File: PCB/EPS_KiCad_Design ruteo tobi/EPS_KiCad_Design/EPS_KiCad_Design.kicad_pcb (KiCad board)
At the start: 4 copper layers, 90 x 90.2 mm, 137 parts, among them IC1 INA226AIDGST, IC10 TPS2553QDBVRQ1, IC11 INA226AIDGST, IC2 TPS2553QDBVRQ1, IC3 INA226AIDGST, IC4 TPS2553QDBVRQ1, IC5 AP63205WU-7, IC6 STM32L433CBT7, IC7 LT3652IMSE#PBF, IC8 INA226AIDGST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

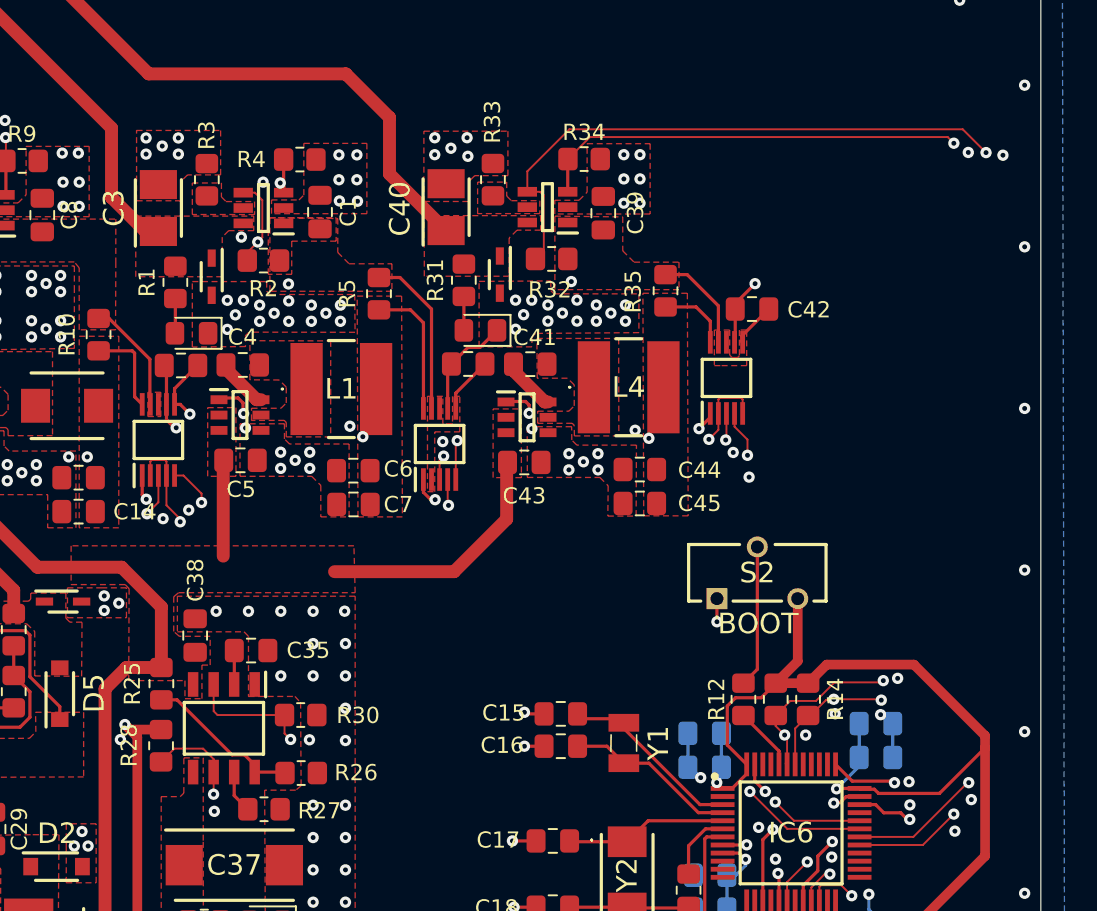
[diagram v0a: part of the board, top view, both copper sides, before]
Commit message: Agregue nombres al pcb
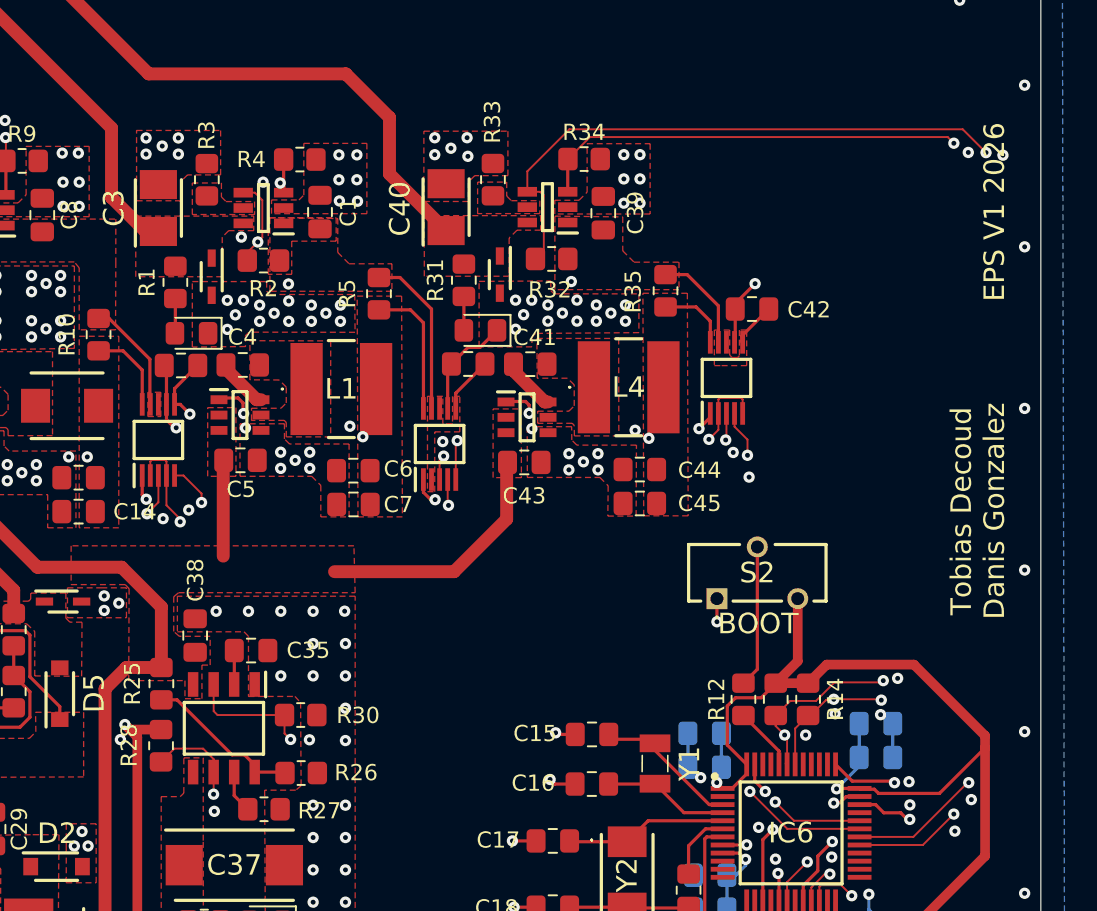
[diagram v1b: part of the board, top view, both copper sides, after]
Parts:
- moved C16 3.03 mm to (162.2, 117.2)
- moved Y1 2.31 mm to (166.1, 116.0)
- moved C15 2.31 mm to (162.2, 114.2)
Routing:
- net /MCU/PC15: track 10.7 -> 7.88 mm
- net /MCU/PC14: track 11.6 -> 9.17 mm
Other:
- board text added: "EPS V1 2026"
- board text added: "Tobias Decoud Danis Gonzalez"
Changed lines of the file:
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@@
 	(footprint "ABS07-LR-32.768KHZ-6-1-T_Footprint:ABS07LR32768kHz61T"
 		(layer "F.Cu")
-		(at 164.2 114.7 -90)
+		(at 166.13 115.97 -90)
 		(descr "ABS07-LR-32.768kHz-6-1-T-2")
 		(tags "Crystal or Oscillator")
@@
 	(footprint "Capacitor_SMD:C_0805_2012Metric_Pad1.18x1.45mm_HandSolder"
 		(layer "F.Cu")
-		(at 160.3 112.9)
+		(at 162.23 114.17)
 		(descr "Capacitor SMD 0805 (2012 Metric), square (rectangular) end terminal, IPC-7351 nominal with elongated pad for handsoldering. (Body size source: IPC-SM-782 page 76, https://www.pcb-3d.com/wordpress/wp-content/uploads/ipc-sm-782a_amendment_1_and_2.pdf, https://docs.google.com/spreadsheets/d/1BsfQQcO9C6DZCsRaXUlFlo91Tg2WpOkGARC1WS5S8t0/edit?usp=sharing), generated with kicad-footprint-generator")
 		(tags "capacitor handsolder")
@@
 	(footprint "Capacitor_SMD:C_0805_2012Metric_Pad1.18x1.45mm_HandSolder"
 		(layer "F.Cu")
-		(at 160.3 114.9)
+		(at 162.22 117.24)
 		(descr "Capacitor SMD 0805 (2012 Metric), square (rectangular) end terminal, IPC-7351 nominal with elongated pad for handsoldering. (Body size source: IPC-SM-782 page 76, https://www.pcb-3d.com/wordpress/wp-content/uploads/ipc-sm-782a_amendment_1_and_2.pdf, https://docs.google.com/spreadsheets/d/1BsfQQcO9C6DZCsRaXUlFlo91Tg2WpOkGARC1WS5S8t0/edit?usp=sharing), generated with kicad-footprint-generator")
 		(tags "capacitor handsolder")
@@
 		)
 	)
+	(gr_text "EPS V1 2026"
+		(at 187.13 81.84 90)
+		(layer "F.SilkS")
+		(effects
+			(font
+				(size 1.27 1.27)
+				(thickness 0.254)
+			)
+		)
+	)
 	(gr_text "3V3"
 		(at 177.92 141.961905 90)
@@
 		)
 	)
+	(gr_text "Tobias Decoud\nDanis Gonzalez"
+		(at 186.107685 100.35 90)
+		(layer "F.SilkS")
+		(effects
+			(font
+				(size 1.27 1.27)
+				(thickness 0.254)
+			)
+		)
+	)
 	(gr_text "EN\nOBC"
 		(at 156.46 67.69 0)
@@
 	)
 	(segment
+		(start 161.1825 117.24)
+		(end 159.92 117.24)
+		(width 0.2)
+		(layer "F.Cu")
+		(net 14)
+	)
+	(segment
 		(start 185.08 127.99)
 		(end 185.09 127.98)
@@
 	)
 	(segment
-		(start 158.15 112.9)
-		(end 158.05 112.8)
+		(start 160.08 114.17)
+		(end 159.98 114.07)
 		(width 0.2)
 		(layer "F.Cu")
@@
 	)
 	(segment
-		(start 159.2625 114.9)
-		(end 158.05 114.9)
-		(width 0.2)
-		(layer "F.Cu")
-		(net 14)
-	)
-	(segment
 		(start 136.501415 95.2)
 		(end 136.398 95.2)
@@
 	)
 	(segment
-		(start 159.2625 112.9)
-		(end 158.15 112.9)
+		(start 159.92 117.24)
+		(end 159.64 116.96)
+		(width 0.2)
+		(layer "F.Cu")
+		(net 14)
+	)
+	(segment
+		(start 161.1925 114.17)
+		(end 160.08 114.17)
 		(width 0.2)
 		(layer "F.Cu")
@@
 	)
 	(via
-		(at 158.05 114.9)
+		(at 159.64 116.96)
 		(size 0.7)
 		(drill 0.3)
@@
 	)
 	(via
-		(at 158.05 112.8)
+		(at 159.98 114.07)
 		(size 0.7)
 		(drill 0.3)
@@
 	)
 	(segment
-		(start 133.93 90.58)
-		(end 133.785 90.435)
+		(start 134.4 91.62)
+		(end 133.215 90.435)
 		(width 0.2)
 		(layer "F.Cu")
@@
 	(segment
 		(start 134.4 93.75)
-		(end 133.93 93.28)
+		(end 134.4 91.62)
 		(width 0.2)
 		(layer "F.Cu")
@@
 	)
 	(segment
-		(start 133.785 90.435)
+		(start 133.215 90.435)
 		(end 131.7 90.435)
 		(width 0.2)
@@
 	)
 	(segment
-		(start 133.93 93.28)
-		(end 133.93 90.58)
-		(width 0.2)
-		(layer "F.Cu")
-		(net 22)
-	)
-	(segment
 		(start 122.85 93.835)
 		(end 123.185 93.835)
@@
 	)
 	(segment
-		(start 164.2 113.45)
-		(end 163.95 113.2)
+		(start 166.13 114.72)
+		(end 165.88 114.47)
 		(width 0.2)
 		(layer "F.Cu")
@@
 	)
 	(segment
-		(start 164.15 113.4)
-		(end 164.2 113.45)
+		(start 166.13 115.159)
+		(end 166.13 114.72)
 		(width 0.2)
 		(layer "F.Cu")
@@
 	)
 	(segment
-		(start 164.2 113.8)
-		(end 168.912 118.512)
+		(start 166.08 114.67)
+		(end 166.13 114.72)
 		(width 0.2)
 		(layer "F.Cu")
@@
 	)
 	(segment
-		(start 164.2 113.45)
-		(end 164.2 113.8)
+		(start 170.312 118.512)
+		(end 169.483 118.512)
 		(width 0.2)
 		(layer "F.Cu")
@@
 	)
 	(segment
-		(start 168.912 118.512)
-		(end 170.312 118.512)
+		(start 163.5675 114.47)
+		(end 163.2675 114.17)
 		(width 0.2)
 		(layer "F.Cu")
@@
 	)
 	(segment
-		(start 161.6375 113.2)
-		(end 161.3375 112.9)
+		(start 169.483 118.512)
+		(end 166.13 115.159)
 		(width 0.2)
 		(layer "F.Cu")
@@
 	)
 	(segment
-		(start 163.95 113.2)
-		(end 161.6375 113.2)
+		(start 165.88 114.47)
+		(end 163.5675 114.47)
 		(width 0.2)
 		(layer "F.Cu")
@@
 	)
 	(segment
-		(start 164.2 115.95)
-		(end 165.75 115.95)
-		(width 0.2)
-		(layer "F.Cu")
-		(net 30)
-	)
-	(segment
-		(start 164.15 116)
-		(end 164.2 115.95)
+		(start 167.922 119.012)
+		(end 170.312 119.012)
 		(width 0.2)
 		(layer "F.Cu")
@@
 	)
 	(segment
-		(start 165.75 115.95)
-		(end 168.812 119.012)
+		(start 166.13 117.22)
+		(end 167.922 119.012)
 		(width 0.2)
 		(layer "F.Cu")
@@
 	)
 	(segment
-		(start 163.15 114.9)
-		(end 161.3375 114.9)
+		(start 166.08 117.27)
+		(end 166.13 117.22)
 		(width 0.2)
 		(layer "F.Cu")
@@
 	)
 	(segment
-		(start 164.2 115.95)
-		(end 163.15 114.9)
+		(start 163.2575 117.24)
+		(end 166.11 117.24)
 		(width 0.2)
 		(layer "F.Cu")
@@
 	)
 	(segment
-		(start 168.812 119.012)
-		(end 170.312 119.012)
+		(start 166.11 117.24)
+		(end 166.13 117.22)
 		(width 0.2)
 		(layer "F.Cu")
